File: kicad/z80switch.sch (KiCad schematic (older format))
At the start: 60 parts, among them CON1 BARREL_JACK, P1 CONN_01X02, P2 CONN_01X03, SW1 SW_PUSH, SW10 SWITCH_INV, SW11 SWITCH_INV, SW12 SWITCH_INV, SW13 SWITCH_INV, SW14 SWITCH_INV, SW15 SWITCH_INV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

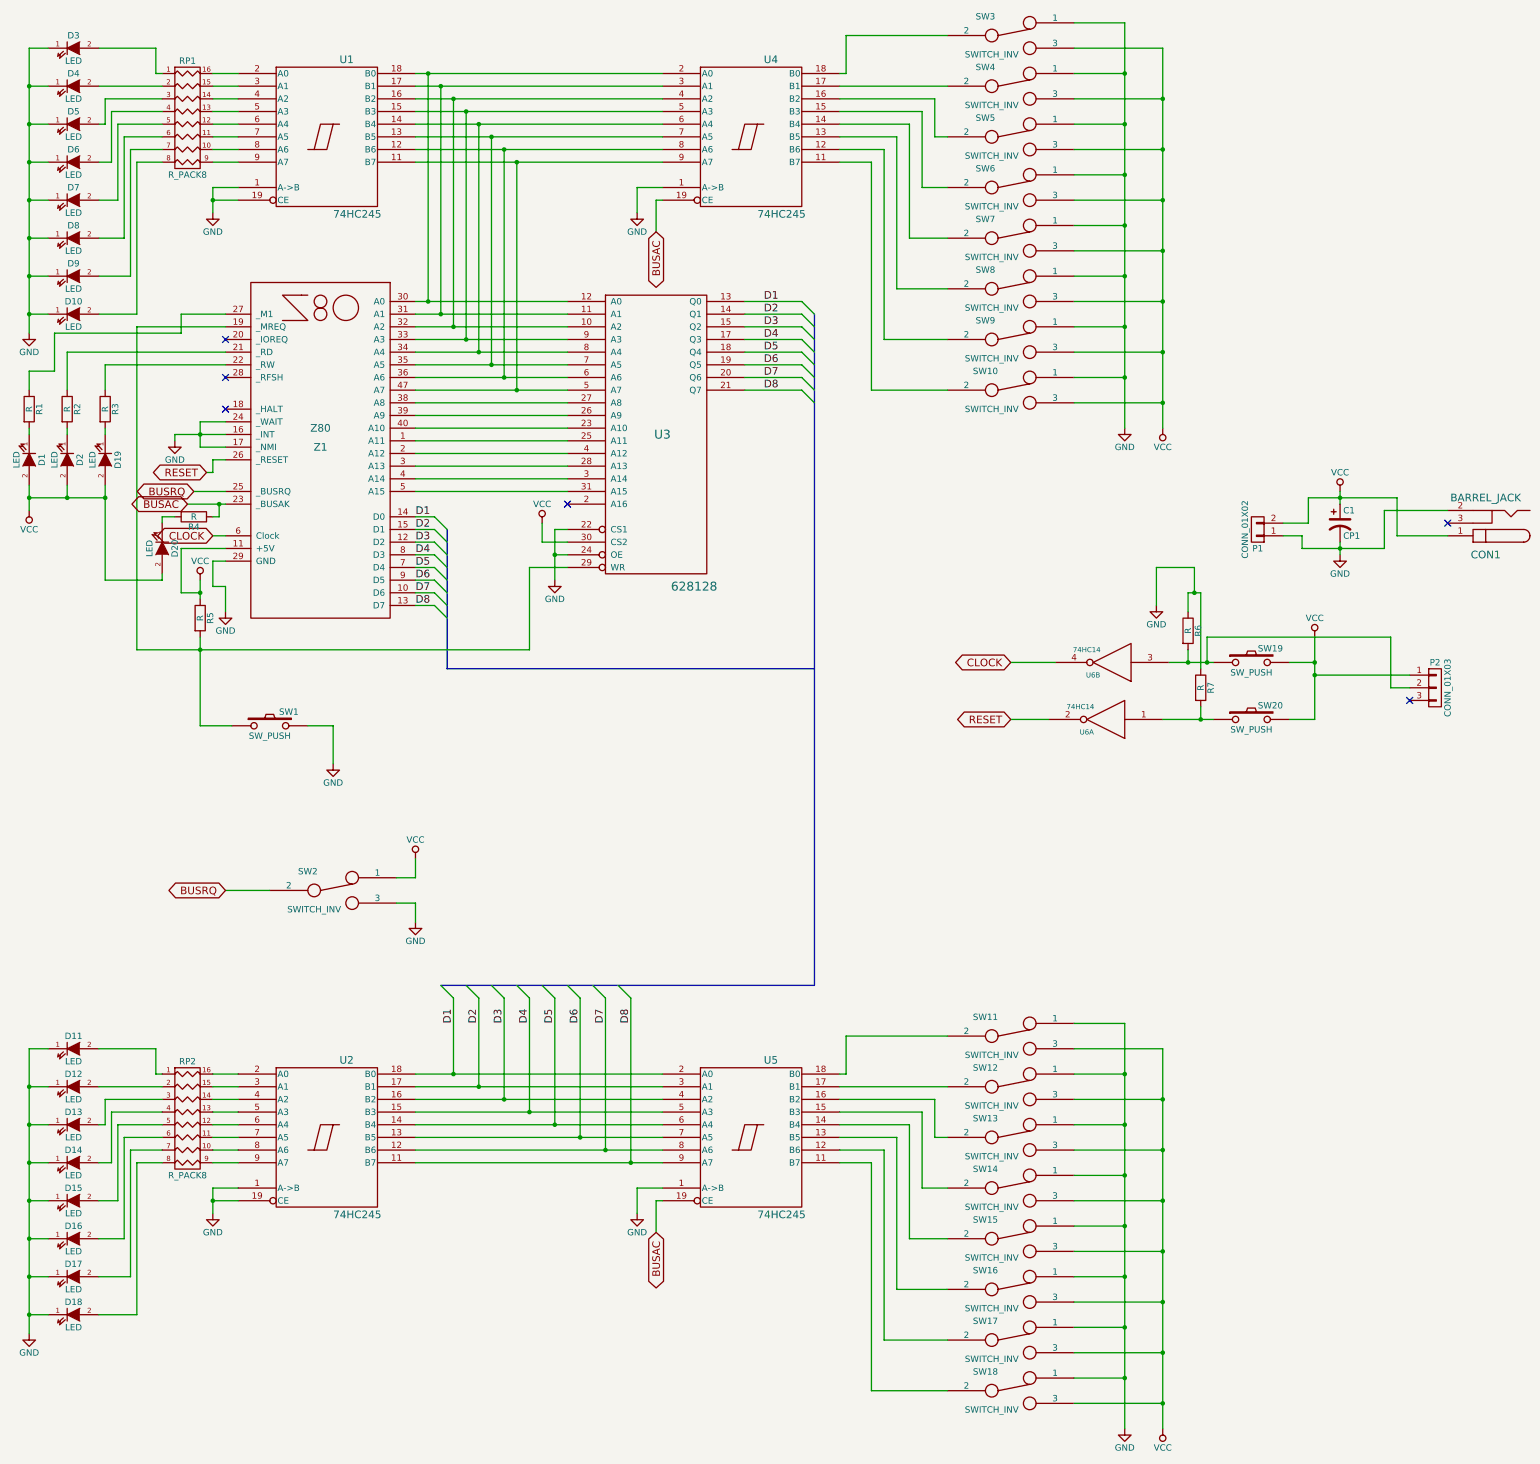
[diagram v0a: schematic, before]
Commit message: Correct read/write lines and debounced inputs
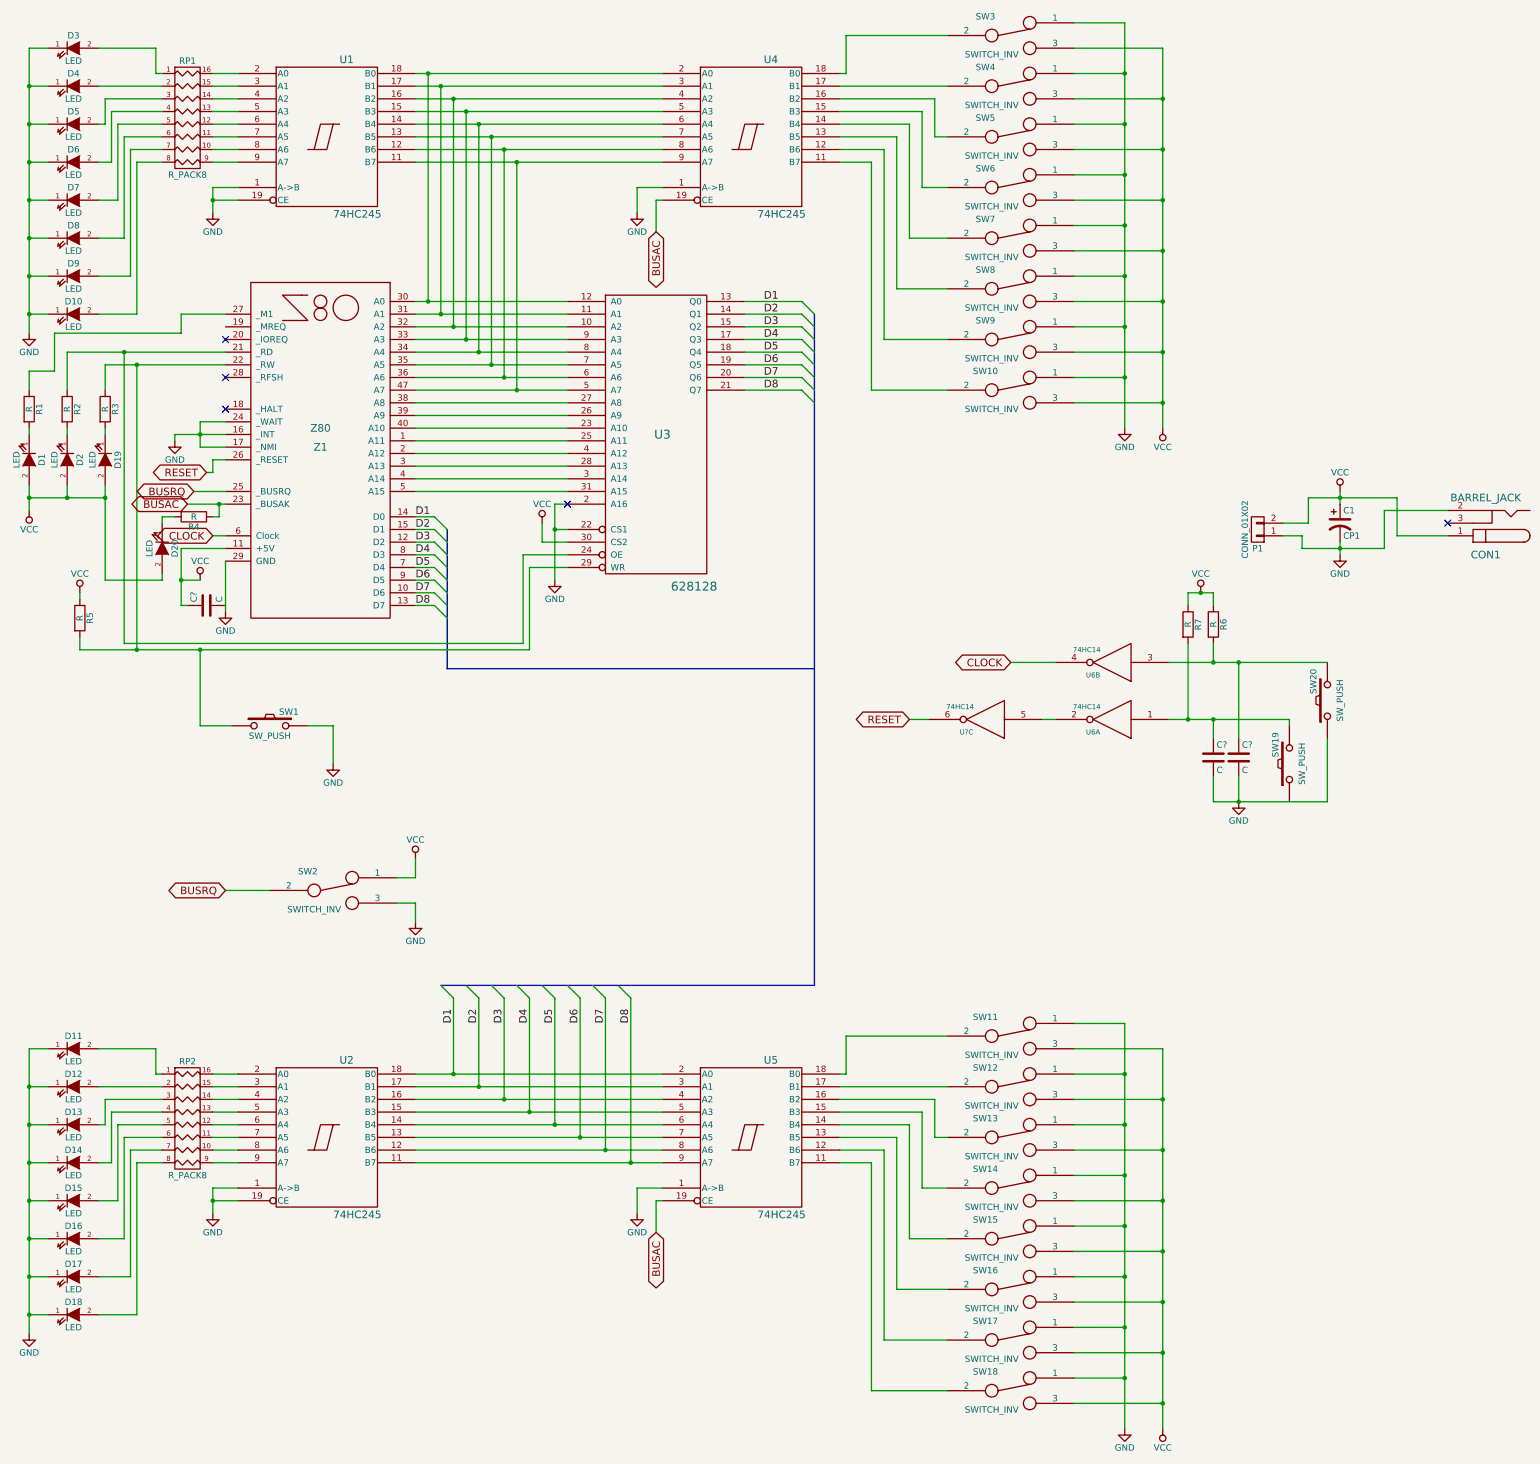
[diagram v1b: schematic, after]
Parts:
- removed P2: CONN_01X03, symbol CONN_01X03
- added C? (x3): C, symbol C
- added U?: 74HC14, symbol 74HC14
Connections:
- net GND: now also SW20.1, U3.2 (A16), C?.2, C?.2, U?.7 (GND); no longer R6.1, R7.1, U3.24 (OE)
- net RESET: now also U?.6; no longer U6.2
- net VCC: now also R6.1, R7.1, C?.1, U?.14 (VCC); no longer SW19.2, SW20.2
- net at R5.2, SW1.1, U3.29 (WR): now also R3.1, Z1.22 (_RW); no longer Z1.19 (_MREQ)
- net at R2.1, Z1.21 (_RD): now also U3.24 (OE)
- net at R6.2, U6.3: now also SW20.2, C?.1; no longer SW19.1
- net at R7.2, U6.1: now also SW19.2, C?.1; no longer SW20.1
- new net: U6.2, U?.5
- no-connect marks 6 -> 5
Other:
- moved on the sheet: R5, R6, R7, SW19, SW20, U6A
